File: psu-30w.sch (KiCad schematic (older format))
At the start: 40 parts, among them J1 Barrel_Jack, J101 SWITCH, U1 R-78E5.0-1.0

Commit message: Gerbers
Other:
- moved on the sheet: C3, D5, R4, U1
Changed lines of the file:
@@
 L Device:CP C3
 U 1 1 5B7395F5
-P 6000 4650
-F 0 "C3" H 6118 4696 50  0000 L CNN
-F 1 "22u" H 6118 4605 50  0000 L CNN
-F 2 "Capacitor_SMD:CP_Elec_10x10" H 6038 4500 50  0001 C CNN
-F 3 "~" H 6000 4650 50  0001 C CNN
-	1    6000 4650
+P 6400 4450
+F 0 "C3" H 6518 4496 50  0000 L CNN
+F 1 "22u" H 6518 4405 50  0000 L CNN
+F 2 "Capacitor_SMD:CP_Elec_10x10" H 6438 4300 50  0001 C CNN
+F 3 "~" H 6400 4450 50  0001 C CNN
+	1    6400 4450
 	1    0    0    -1
 $EndComp
 Wire Wire Line
-	6000 4000 6000 4500
+	6400 4000 6400 4300
 Wire Wire Line
-	6000 4950 6000 4800
+	6400 4950 6400 4600
 $Comp
 L Device:R R4
 U 1 1 5B73AA82
-P 6500 4000
-F 0 "R4" V 6293 4000 50  0000 C CNN
-F 1 "180" V 6384 4000 50  0000 C CNN
-F 2 "Resistor_SMD:R_0805_2012Metric_Pad1.15x1.40mm_HandSolder" V 6430 4000 50  0001 C CNN
-F 3 "~" H 6500 4000 50  0001 C CNN
-	1    6500 4000
+P 6800 4000
+F 0 "R4" V 6593 4000 50  0000 C CNN
+F 1 "180" V 6684 4000 50  0000 C CNN
+F 2 "Resistor_SMD:R_0805_2012Metric_Pad1.15x1.40mm_HandSolder" V 6730 4000 50  0001 C CNN
+F 3 "~" H 6800 4000 50  0001 C CNN
+	1    6800 4000
 	0    1    1    0
 $EndComp
 Wire Wire Line
-	6000 4000 6350 4000
+	6400 4000 6650 4000
 $Comp
 L Device:LED D5
 U 1 1 5B73B5BD
-P 6800 4400
-F 0 "D5" V 6838 4283 50  0000 R CNN
-F 1 "LED" V 6747 4283 50  0000 R CNN
-F 2 "LED_THT:LED_D5.0mm" H 6800 4400 50  0001 C CNN
-F 3 "~" H 6800 4400 50  0001 C CNN
-	1    6800 4400
+P 7200 4400
+F 0 "D5" V 7238 4283 50  0000 R CNN
+F 1 "LED" V 7147 4283 50  0000 R CNN
+F 2 "LED_THT:LED_D5.0mm" H 7200 4400 50  0001 C CNN
+F 3 "~" H 7200 4400 50  0001 C CNN
+	1    7200 4400
 	0    -1   -1   0
 $EndComp
 Wire Wire Line
-	6650 4000 6800 4000
+	6950 4000 7200 4000
 Wire Wire Line
-	6800 4000 6800 4250
+	7200 4000 7200 4250
 Wire Wire Line
-	6800 4550 6800 4950
+	7200 4550 7200 4950
 Wire Wire Line
-	6800 4950 6400 4950
+	7200 4950 6800 4950
 $Comp
 L Connector_Generic:Conn_02x08_Odd_Even J2
@@
 	2150 1950 2650 1950
 $Comp
-L power:PWR_FLAG #FLG0101
-U 1 1 5B96B47C
-P 3800 3900
-F 0 "#FLG0101" H 3800 3975 50  0001 C CNN
-F 1 "PWR_FLAG" H 3800 4074 50  0000 C CNN
-F 2 "" H 3800 3900 50  0001 C CNN
-F 3 "~" H 3800 3900 50  0001 C CNN
-	1    3800 3900
-	1    0    0    -1
-$EndComp
-Wire Wire Line
-	3800 4000 3800 3900
-$Comp
 L dcdc:DKA30A-12 DC101
 U 1 1 5B9B7520
@@
 L Regulator_Linear:L7805 U1
 U 1 1 5CACEEB5
-P 4800 4000
-F 0 "U1" H 4800 4242 50  0000 C CNN
-F 1 "R-78E5.0-1.0" H 4800 4151 50  0000 C CNN
-F 2 "Package_SIP:SIP3_11.6x8.5mm" H 4825 3850 50  0001 L CIN
-F 3 "http://www.st.com/content/ccc/resource/technical/document/datasheet/41/4f/b3/b0/12/d4/47/88/CD00000444.pdf/files/CD00000444.pdf/jcr:content/translations/en.CD00000444.pdf" H 4800 3950 50  0001 C CNN
-	1    4800 4000
+P 5550 4000
+F 0 "U1" H 5550 4242 50  0000 C CNN
+F 1 "R-78E5.0-1.0" H 5550 4151 50  0000 C CNN
+F 2 "Package_SIP:SIP3_11.6x8.5mm" H 5575 3850 50  0001 L CIN
+F 3 "http://www.st.com/content/ccc/resource/technical/document/datasheet/41/4f/b3/b0/12/d4/47/88/CD00000444.pdf/files/CD00000444.pdf/jcr:content/translations/en.CD00000444.pdf" H 5550 3950 50  0001 C CNN
+	1    5550 4000
 	1    0    0    -1
 $EndComp
 Wire Wire Line
-	5100 4000 6000 4000
-Connection ~ 6000 4000
+	5850 4000 6400 4000
+Connection ~ 6400 4000
 $Comp
 L power:GND #PWR0106
 U 1 1 5CB1C44F
-P 4800 4500
-F 0 "#PWR0106" H 4800 4250 50  0001 C CNN
-F 1 "GND" H 4805 4327 50  0000 C CNN
-F 2 "" H 4800 4500 50  0001 C CNN
-F 3 "" H 4800 4500 50  0001 C CNN
-	1    4800 4500
+P 5550 4500
+F 0 "#PWR0106" H 5550 4250 50  0001 C CNN
+F 1 "GND" H 5555 4327 50  0000 C CNN
+F 2 "" H 5550 4500 50  0001 C CNN
+F 3 "" H 5550 4500 50  0001 C CNN
+	1    5550 4500
 	1    0    0    -1
 $EndComp
 Wire Wire Line
-	4800 4300 4800 4500
+	5550 4300 5550 4500
 $Comp
 L power:GND #PWR0299
 U 1 1 5CB47BBC
-P 6400 5050
-F 0 "#PWR0299" H 6400 4800 50  0001 C CNN
-F 1 "GND" H 6405 4877 50  0000 C CNN
-F 2 "" H 6400 5050 50  0001 C CNN
-F 3 "" H 6400 5050 50  0001 C CNN
-	1    6400 5050
+P 6800 5050
+F 0 "#PWR0299" H 6800 4800 50  0001 C CNN
+F 1 "GND" H 6805 4877 50  0000 C CNN
+F 2 "" H 6800 5050 50  0001 C CNN
+F 3 "" H 6800 5050 50  0001 C CNN
+	1    6800 5050
 	1    0    0    -1
 $EndComp
 Wire Wire Line
-	6400 4950 6400 5050
-Connection ~ 6400 4950
+	6800 4950 6800 5050
+Connection ~ 6800 4950
 Wire Wire Line
-	6400 4950 6000 4950
+	6800 4950 6400 4950
 $Comp
 L power:+5V #PWR0300
 U 1 1 5CB9B154
-P 6000 3800
-F 0 "#PWR0300" H 6000 3650 50  0001 C CNN
-F 1 "+5V" V 6015 3928 50  0000 L CNN
-F 2 "" H 6000 3800 50  0001 C CNN
-F 3 "" H 6000 3800 50  0001 C CNN
-	1    6000 3800
+P 6400 3800
+F 0 "#PWR0300" H 6400 3650 50  0001 C CNN
+F 1 "+5V" V 6415 3928 50  0000 L CNN
+F 2 "" H 6400 3800 50  0001 C CNN
+F 3 "" H 6400 3800 50  0001 C CNN
+	1    6400 3800
 	-1   0    0    -1
 $EndComp
 Wire Wire Line
-	6000 3800 6000 4000
+	6400 3800 6400 4000
 Wire Wire Line
 	5200 1750 5600 1750
@@
 Wire Wire Line
 	3750 2050 4050 2050
-Wire Wire Line
-	3800 4000 4250 4000
 $Comp
 L Jumper:Jumper_3_Open JP2
@@
 $EndComp
 Wire Wire Line
-	4850 3100 4850 3300
-Wire Wire Line
-	4850 3300 4250 3300
-Wire Wire Line
-	4250 3300 4250 4000
-Connection ~ 4250 4000
-Wire Wire Line
-	4250 4000 4500 4000
-Wire Wire Line
 	5100 2950 5600 2950
 Wire Wire Line
@@
 Wire Wire Line
 	3750 1400 3750 1500
+Wire Wire Line
+	4600 4000 4600 3900
+$Comp
+L power:PWR_FLAG #FLG0101
+U 1 1 5B96B47C
+P 4600 3900
+F 0 "#FLG0101" H 4600 3975 50  0001 C CNN
+F 1 "PWR_FLAG" H 4600 4074 50  0000 C CNN
+F 2 "" H 4600 3900 50  0001 C CNN
+F 3 "~" H 4600 3900 50  0001 C CNN
+	1    4600 3900
+	1    0    0    -1
+$EndComp
+Wire Wire Line
+	4850 4000 5250 4000
+Wire Wire Line
+	4600 4000 4850 4000
+Connection ~ 4850 4000
+Wire Wire Line
+	4850 3100 4850 4000
 $EndSCHEMATC

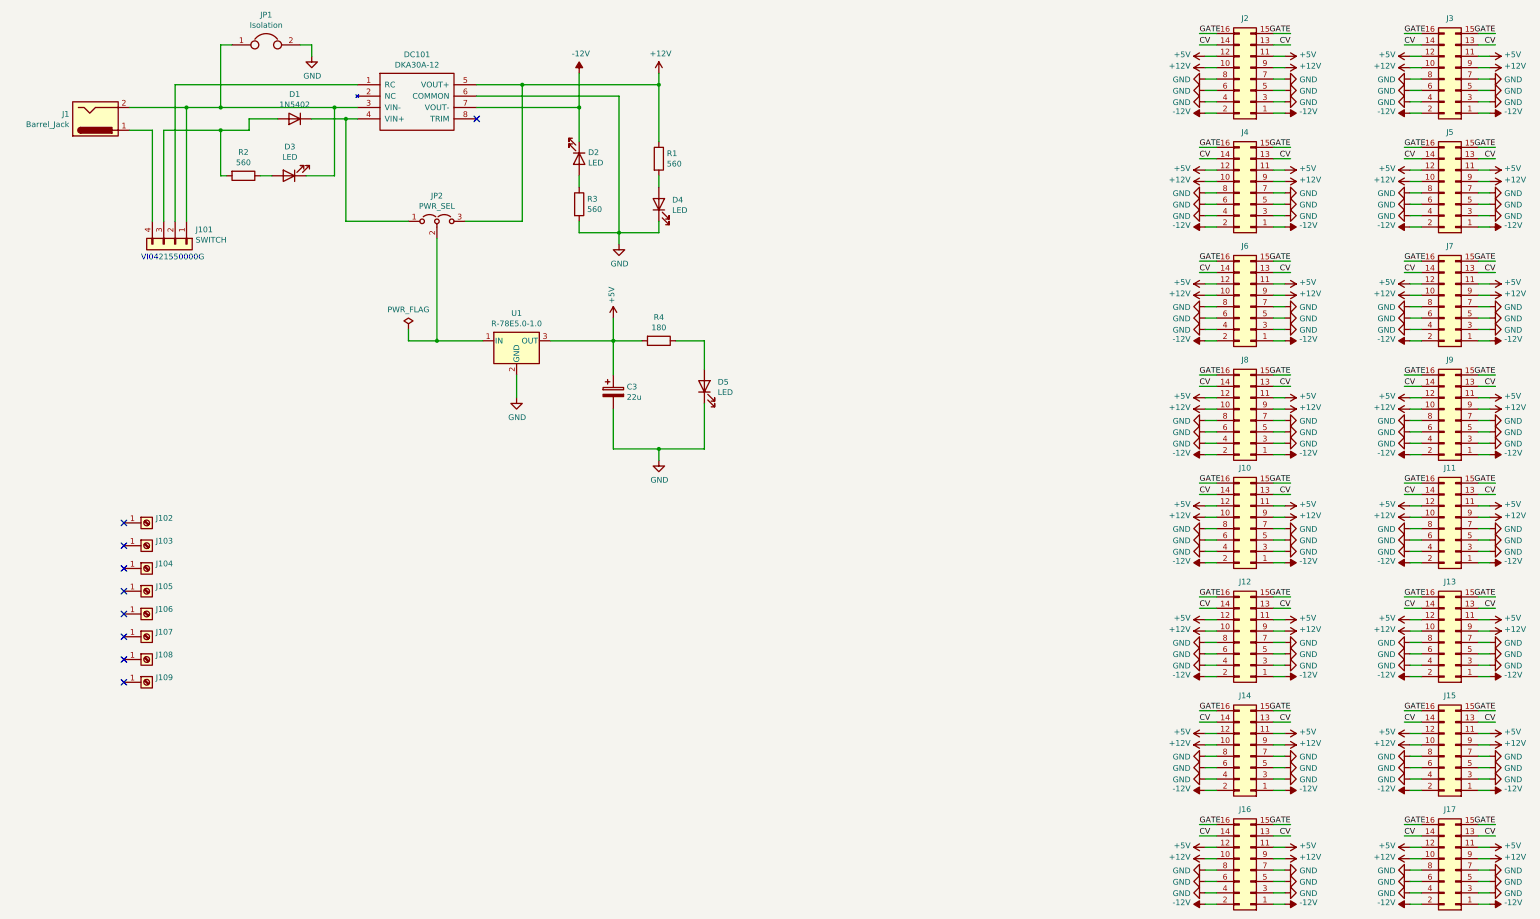
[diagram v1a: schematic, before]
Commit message: adaptations + simplifications
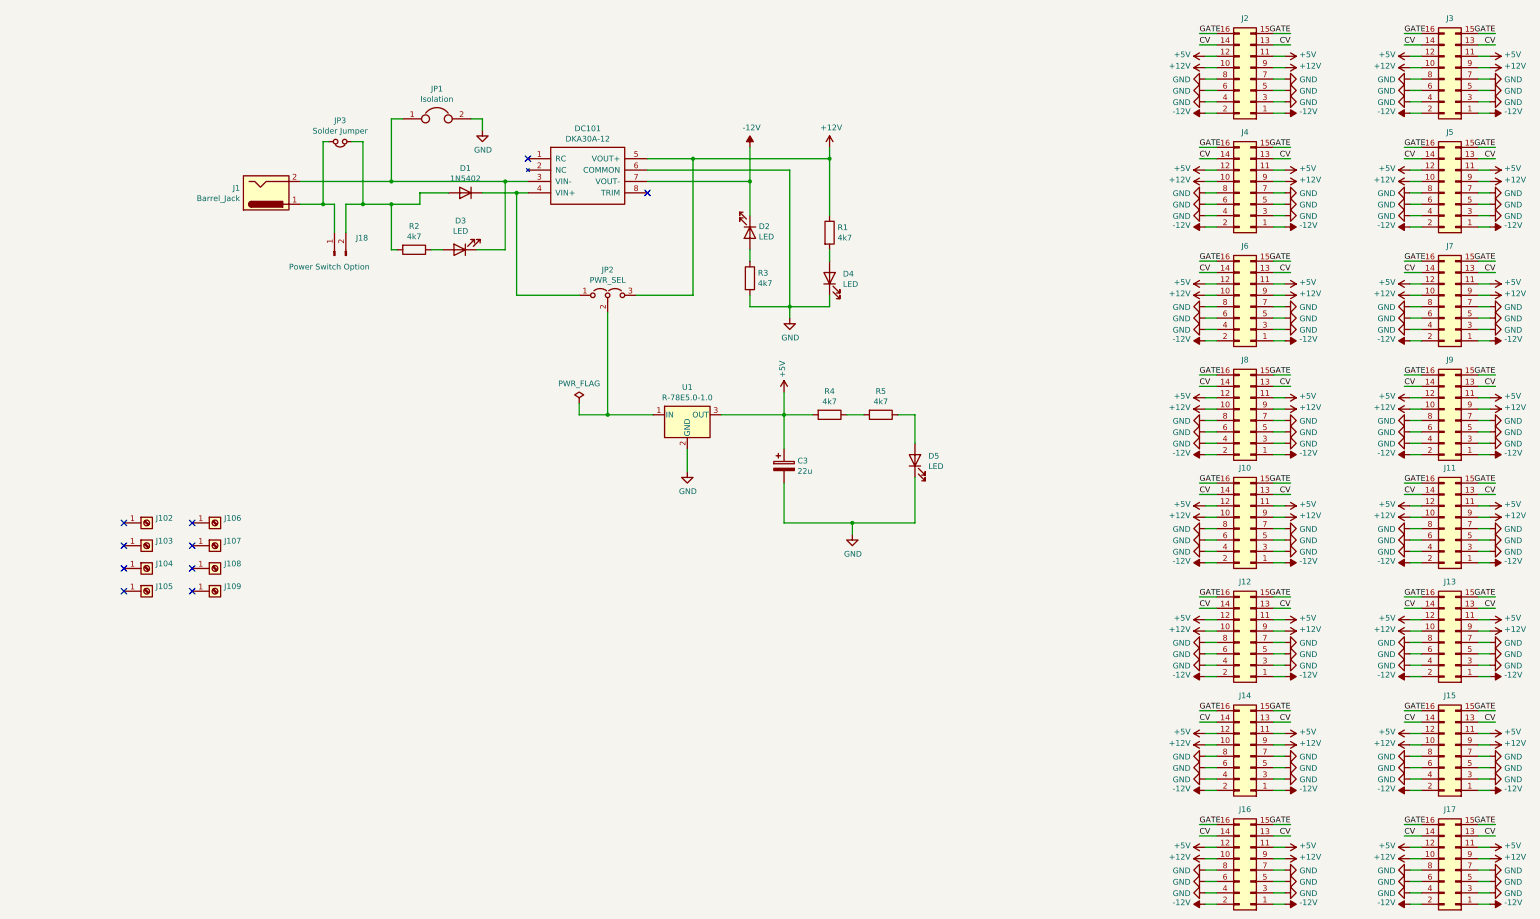
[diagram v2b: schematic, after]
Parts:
- removed J101: SWITCH, Connector_Molex:Molex_KK-254_AE-6410-04A_1x04_P2.54mm_Vertical, symbol Connector_Generic:Conn_01x04
- added J18: Power Switch Option, Connector_PinHeader_2.54mm:PinHeader_1x02_P2.54mm_Vertical, symbol Connector:Conn_01x02_Male
- added JP3: Solder Jumper, Jumper:SolderJumper-2_P1.3mm_Open_TrianglePad1.0x1.5mm, symbol Device:Jumper_NC_Small
- added R5: 4k7, Resistor_SMD:R_0805_2012Metric_Pad1.15x1.40mm_HandSolder, symbol Device:R
- R1, R2, R3: value 560 -> 4k7
- R4: value 180 -> 4k7
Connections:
- net at J1.1: now also J18.1 (Pin_1), JP3.2
- net at D1.2 (A), R2.2: now also J18.2 (Pin_2), JP3.1
- net at R4.1: now also R5.2; no longer D5.2 (A)
- new net: D5.2 (A), R5.1
- no-connect marks 9 -> 10
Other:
- note removed: "VI0421550000G"
- moved on the sheet: C3, D1, D2, D3, D4, D5, DC101, J1, J106, J107, J108, J109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
